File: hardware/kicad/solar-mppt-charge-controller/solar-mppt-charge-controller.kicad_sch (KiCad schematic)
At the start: 0 parts

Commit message: Schematic: LM2596 buck converter power stage complete
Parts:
- added C1: 100uF, symbol Device:C
- added C2: 220uF, symbol Device:C
- added D1, D2: 1N5822, symbol Device:D
- added F1: Fuse, symbol Device:Fuse
- added J1: SOLAR_IN, symbol Connector_Generic:Conn_01x02
- added J2: LOAD_OUT, symbol Connector_Generic:Conn_01x02
- added L1: 100uH, symbol Device:L
- added R1: 100k, symbol Device:R
- added R2: 10k, symbol Device:R
- added U1: LM2596S-ADJ, Package_TO_SOT_SMD:TO-263-5_TabPin3, symbol Regulator_Switching:LM2596S-ADJ
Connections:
- new net: R1.1, R2.1, U1.4 (FB)
- new net: L1.2, U1.2 (OUT)
- new net: D1.2 (A), F1.1, F1.2, J1.1 (Pin_1)
- new net GND: C1.1, C2.2, D2.2 (A), J1.2 (Pin_2), J2.2 (Pin_2), R2.2, U1.3 (GND), U1.5 (~{ON}/OFF)
- new net PANEL_IN: C1.2, D1.1 (K), U1.1 (VIN)
- new net VOUT: C2.1, D2.1 (K), J2.1 (Pin_1), L1.1, R1.2

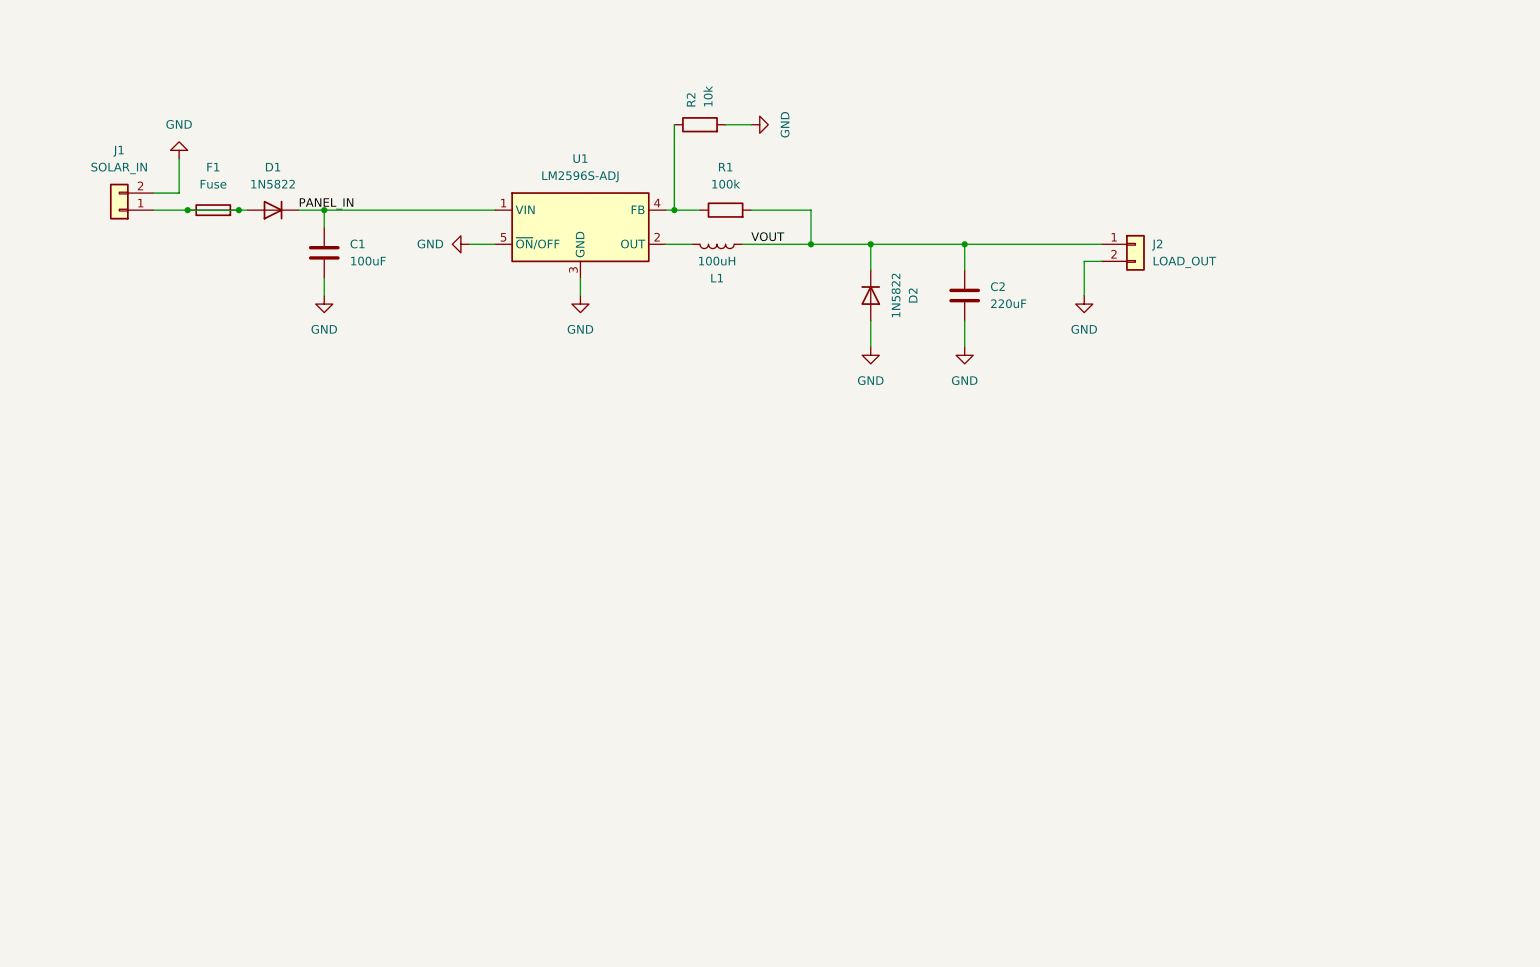
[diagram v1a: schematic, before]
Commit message: Schematic: MCP4131 digital potentiometer complete
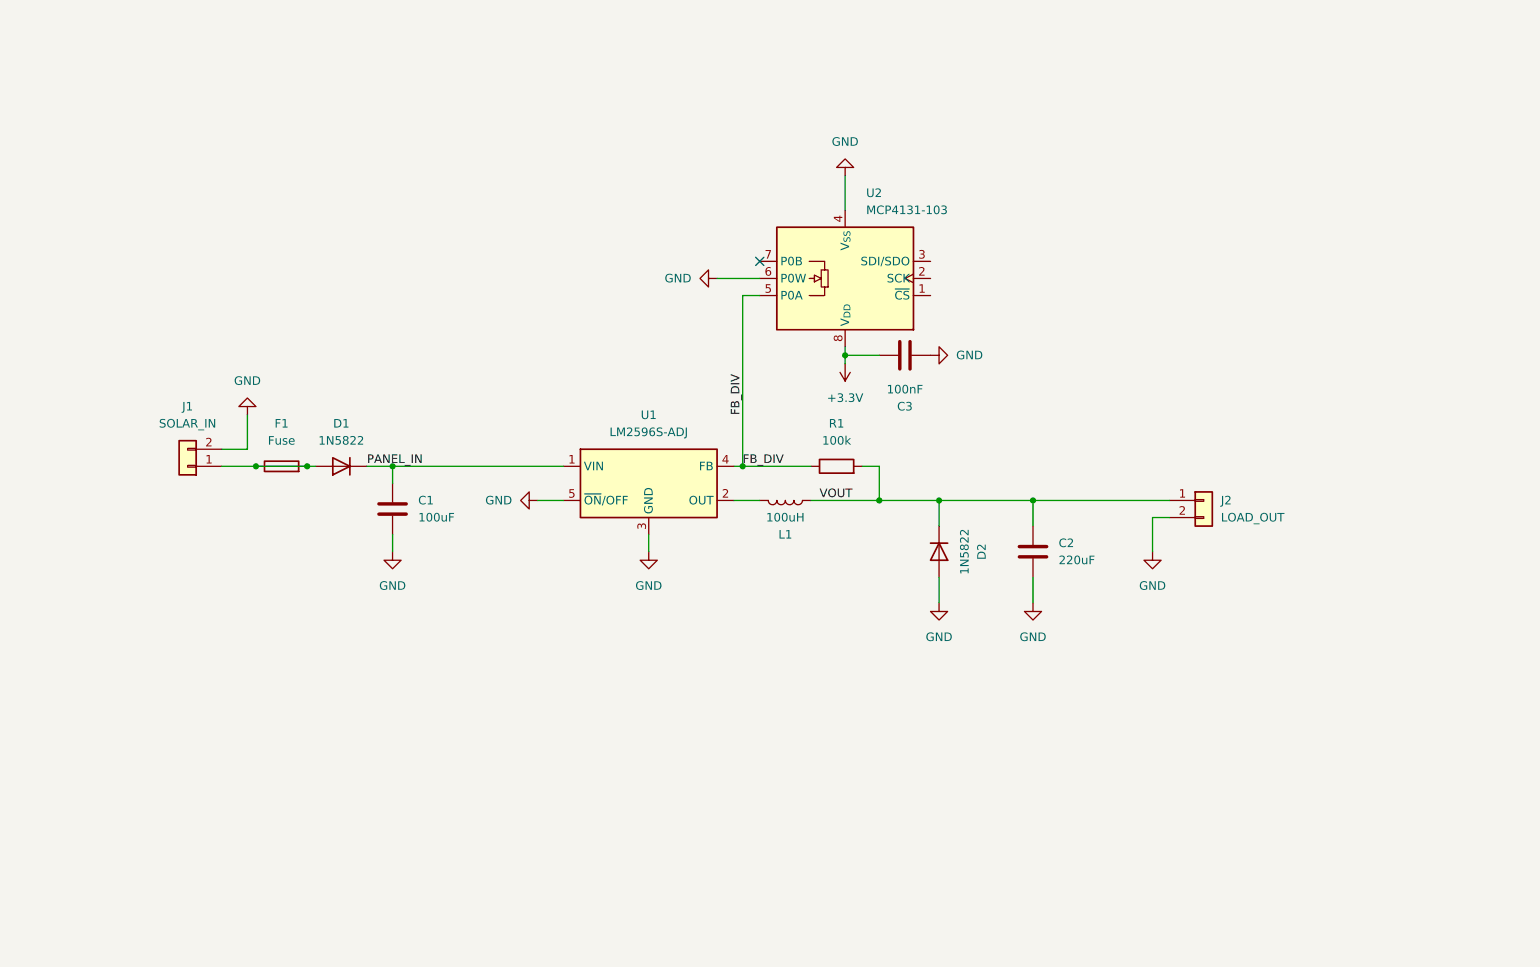
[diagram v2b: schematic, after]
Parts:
- removed R2: 10k, symbol Device:R
- added C3: 100nF, symbol Device:C
- added U2: MCP4131-103, Package_DIP:DIP-8_W7.62mm, symbol Potentiometer_Digital:MCP4131-xxxx-P
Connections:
- net GND: now also C3.1, U2.4 (V_{SS}), U2.6 (P0W)
- net FB_DIV: now reaches R1.1, U1.4 (FB)
- net FB_DIV: now also U2.5 (P0A)
- new net +3.3V: C3.2, U2.8 (V_{DD})
- no-connect marks 0 -> 1
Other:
- moved on the sheet: C1, C2, D1, D2, F1, J1, J2, L1, R1, U1

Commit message: Schematic: ESP32 DevKit connector and UART debug header complete
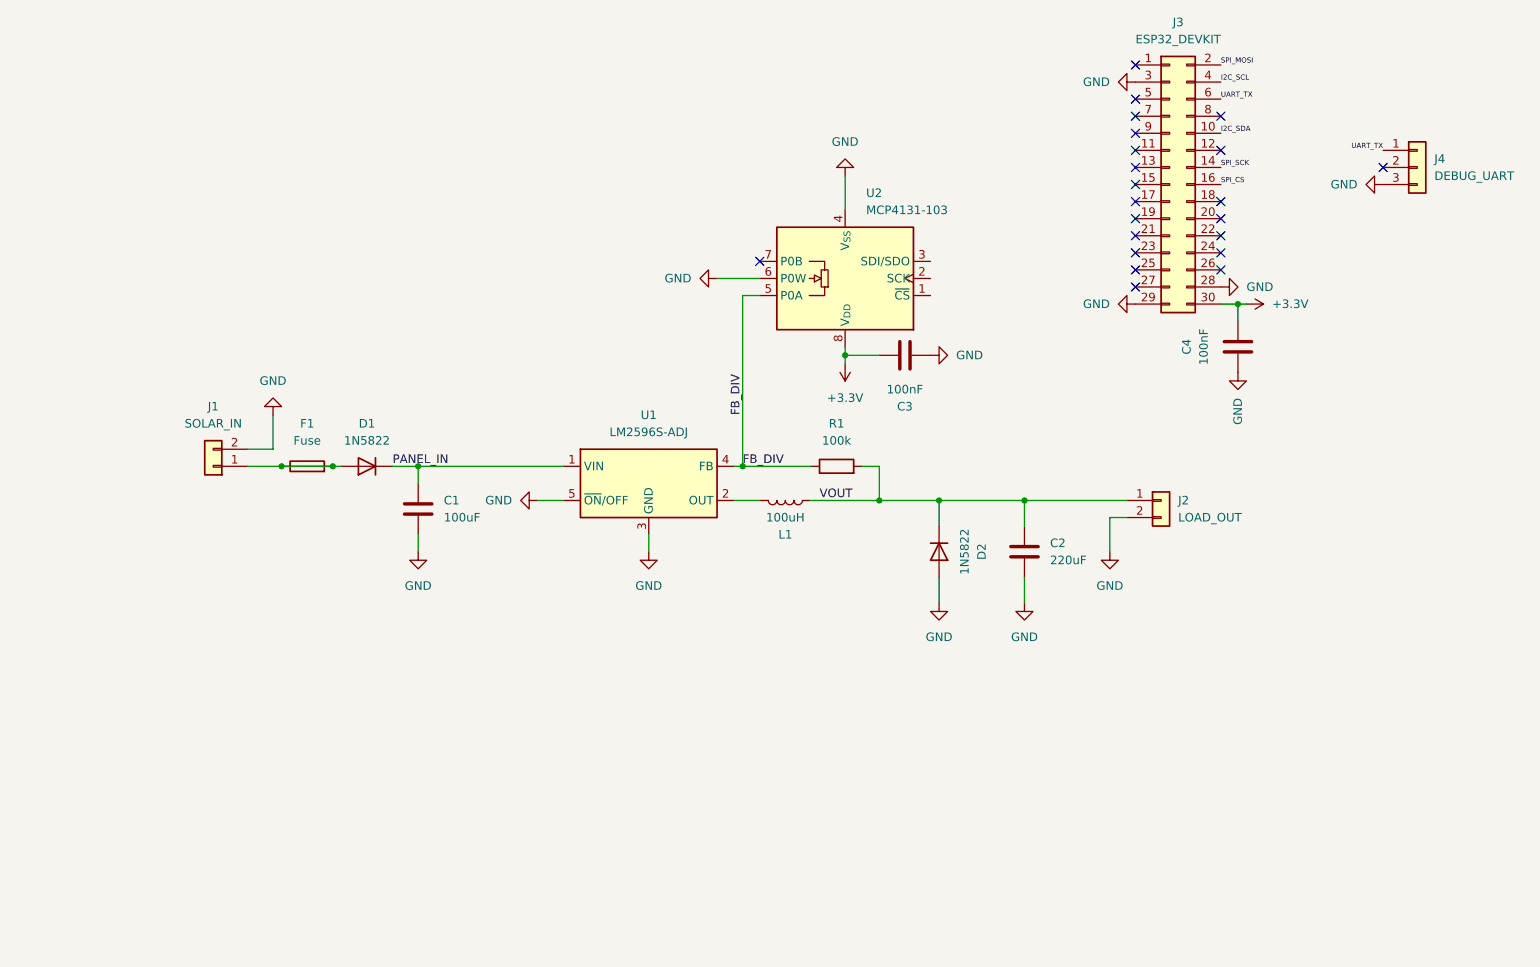
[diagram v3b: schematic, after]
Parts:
- added C4: 100nF, symbol Device:C
- added J3: ESP32_DEVKIT, symbol Connector_Generic:Conn_02x15_Odd_Even
- added J4: DEBUG_UART, symbol Connector_Generic:Conn_01x03
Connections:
- net +3.3V: now also C4.2, J3.30 (Pin_30)
- net GND: now also C4.1, J3.28 (Pin_28), J3.29 (Pin_29), J3.3 (Pin_3), J4.3 (Pin_3)
- new net I2C_SCL: J3.4 (Pin_4)
- new net I2C_SDA: J3.10 (Pin_10)
- new net SPI_CS: J3.16 (Pin_16)
- new net SPI_MOSI: J3.2 (Pin_2)
- new net SPI_SCK: J3.14 (Pin_14)
- new net UART_TX: J3.6 (Pin_6), J4.1 (Pin_1)
- no-connect marks 1 -> 22
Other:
- moved on the sheet: C1, C2, D1, F1, J1, J2

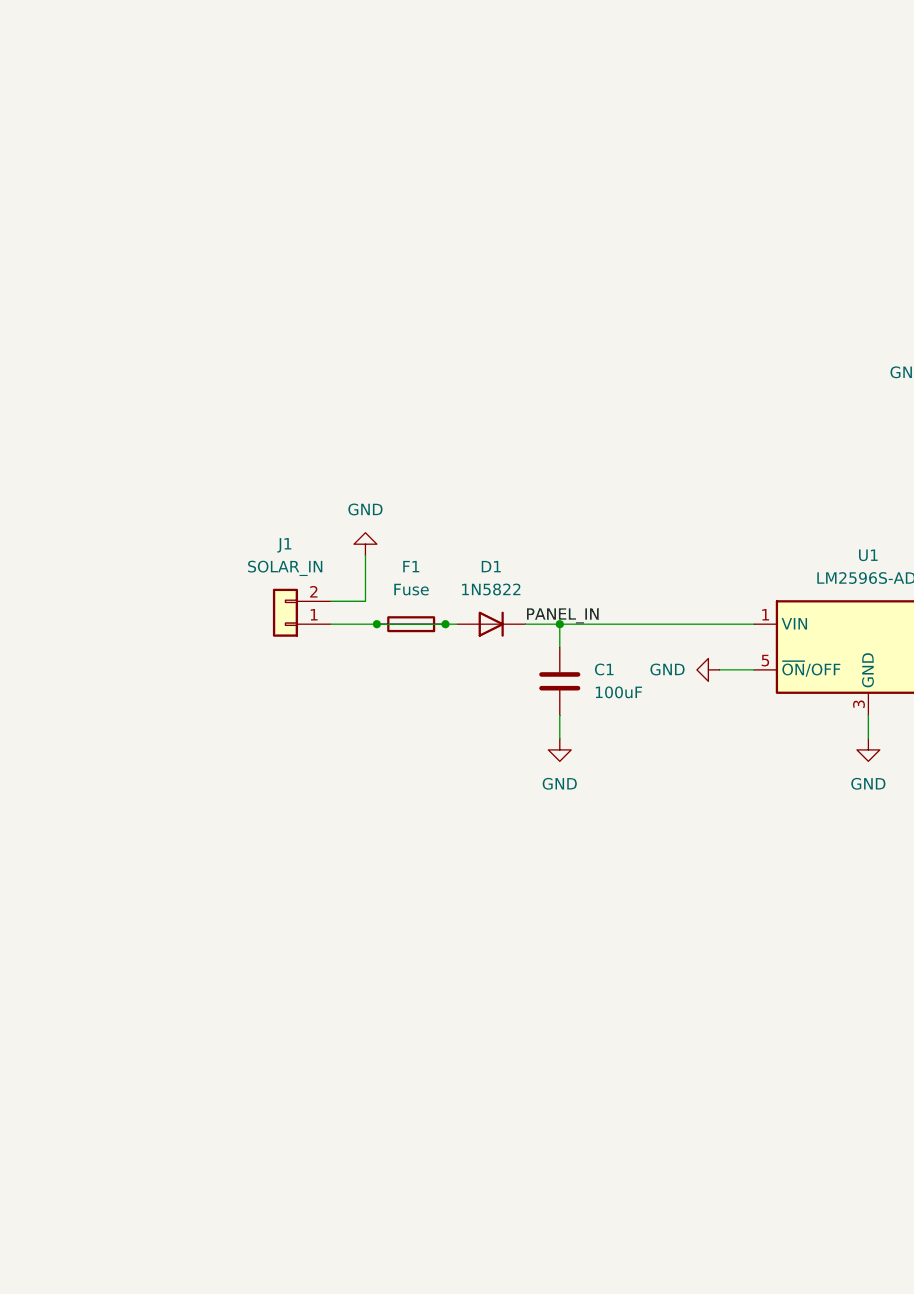
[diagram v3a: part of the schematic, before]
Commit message: Schematic: INA226 panel and load side sensors complete
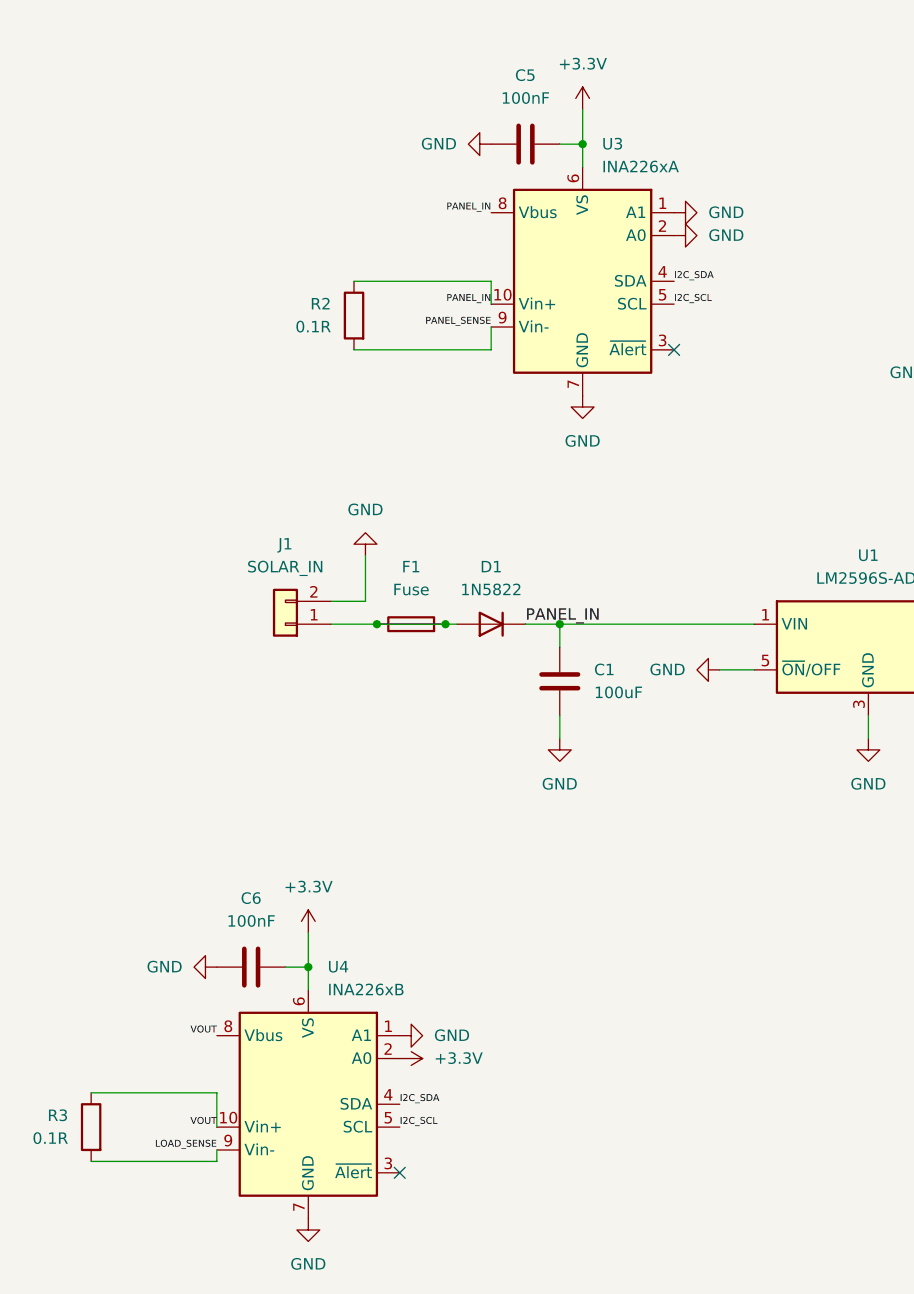
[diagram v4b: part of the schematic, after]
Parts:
- added C5, C6: 100nF, symbol Device:C
- added R2, R3: 0.1R, symbol Device:R
- added U3: INA226xA, Package_SO:TSSOP-10_3x3mm_P0.5mm, symbol Sensor_Energy:INA226
- added U4: INA226xB, Package_SO:TSSOP-10_3x3mm_P0.5mm, symbol Sensor_Energy:INA226
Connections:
- net +3.3V: now also C5.2, C6.2, U3.6 (VS), U4.2 (A0), U4.6 (VS)
- net GND: now also C5.1, C6.1, U3.1 (A1), U3.2 (A0), U3.7 (GND), U4.1 (A1), U4.7 (GND)
- net I2C_SCL: now also U3.5 (SCL), U4.5 (SCL)
- net I2C_SDA: now also U3.4 (SDA), U4.4 (SDA)
- net PANEL_IN: now also R2.1, U3.10 (Vin+), U3.8 (Vbus)
- net VOUT: now also R3.1, U4.10 (Vin+), U4.8 (Vbus)
- new net LOAD_SENSE: R3.2, U4.9 (Vin-)
- new net PANEL_SENSE: R2.2, U3.9 (Vin-)
- no-connect marks 22 -> 24

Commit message: Schematic: ERC clean, zero errors and warnings
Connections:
- net SPI_CS: now also U2.1 (~{CS})
- net SPI_MOSI: now also U2.3 (SDI/SDO)
- net SPI_SCK: now also U2.2 (SCK)

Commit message: Footprints assigned to all schematic components
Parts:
- C1: footprint (none) -> Capacitor_THT:C_Radial_D8.0mm_H7.0mm_P3.50mm
- C2: footprint (none) -> Capacitor_THT:C_Radial_D10.0mm_H12.5mm_P5.00mm
- C3, C4, C5, C6: footprint (none) -> Capacitor_SMD:C_0805_2012Metric_Pad1.18x1.45mm_HandSolder
- D1, D2: footprint (none) -> Diode_THT:D_DO-201AD_P12.70mm_Horizontal
- F1: footprint (none) -> Fuse:Fuse_1812_4532Metric_Pad1.30x3.40mm_HandSolder
- J1, J2: footprint (none) -> Connector_PinHeader_2.54mm:PinHeader_1x02_P2.54mm_Vertical
- J3: footprint (none) -> Connector_PinHeader_2.54mm:PinHeader_2x15_P2.54mm_Vertical
- J4: footprint (none) -> Connector_PinHeader_2.54mm:PinHeader_1x03_P2.54mm_Vertical
- L1: footprint (none) -> Inductor_THT:L_Axial_L11.0mm_D4.5mm_P15.24mm_Horizontal_Fastron_MECC
- R1: footprint (none) -> Resistor_SMD:R_0805_2012Metric_Pad1.20x1.40mm_HandSolder
- R2, R3: footprint (none) -> Resistor_SMD:R_2512_6332Metric_Pad1.40x3.35mm_HandSolder
- U3, U4: footprint Package_SO:TSSOP-10_3x3mm_P0.5mm -> Package_SO:SOIC-10_3.9x4.9mm_P1mm
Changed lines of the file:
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@@
 			)
 		)
-		(property "Footprint" ""
+		(property "Footprint" "Capacitor_THT:C_Radial_D8.0mm_H7.0mm_P3.50mm"
 			(at 104.4448 101.6 0)
 			(hide yes)
@@
 			)
 		)
-		(property "Footprint" ""
+		(property "Footprint" "Resistor_SMD:R_2512_6332Metric_Pad1.40x3.35mm_HandSolder"
 			(at 84.328 64.77 90)
 			(hide yes)
@@
 			)
 		)
-		(property "Footprint" ""
+		(property "Footprint" "Resistor_SMD:R_0805_2012Metric_Pad1.20x1.40mm_HandSolder"
 			(at 167.64 100.838 90)
 			(hide yes)
@@
 			)
 		)
-		(property "Footprint" ""
+		(property "Footprint" "Inductor_THT:L_Axial_L11.0mm_D4.5mm_P15.24mm_Horizontal_Fastron_MECC"
 			(at 160.02 104.14 0)
 			(hide yes)
@@
 			)
 		)
-		(property "Footprint" ""
+		(property "Footprint" "Fuse:Fuse_1812_4532Metric_Pad1.30x3.40mm_HandSolder"
 			(at 88.9 100.838 90)
 			(hide yes)
@@
 			)
 		)
-		(property "Footprint" ""
+		(property "Footprint" "Connector_PinHeader_2.54mm:PinHeader_2x15_P2.54mm_Vertical"
 			(at 217.17 57.15 0)
 			(hide yes)
@@
 			)
 		)
-		(property "Footprint" "Package_SO:TSSOP-10_3x3mm_P0.5mm"
+		(property "Footprint" "Package_SO:SOIC-10_3.9x4.9mm_P1mm"
 			(at 128.27 72.39 0)
 			(hide yes)
@@
 			)
 		)
-		(property "Footprint" ""
+		(property "Footprint" "Diode_THT:D_DO-201AD_P12.70mm_Horizontal"
 			(at 97.79 99.06 0)
 			(hide yes)
@@
 			)
 		)
-		(property "Footprint" ""
+		(property "Footprint" "Capacitor_THT:C_Radial_D10.0mm_H12.5mm_P5.00mm"
 			(at 196.5452 115.57 0)
 			(hide yes)
@@
 			)
 		)
-		(property "Footprint" ""
+		(property "Footprint" "Connector_PinHeader_2.54mm:PinHeader_1x02_P2.54mm_Vertical"
 			(at 215.9 104.14 0)
 			(hide yes)
@@
 			)
 		)
-		(property "Footprint" ""
+		(property "Footprint" "Capacitor_SMD:C_0805_2012Metric_Pad1.18x1.45mm_HandSolder"
 			(at 226.3648 77.47 0)
 			(hide yes)
@@
 			)
 		)
-		(property "Footprint" ""
+		(property "Footprint" "Capacitor_SMD:C_0805_2012Metric_Pad1.18x1.45mm_HandSolder"
 			(at 105.41 44.7548 0)
 			(hide yes)
@@
 			)
 		)
-		(property "Footprint" "Package_SO:TSSOP-10_3x3mm_P0.5mm"
+		(property "Footprint" "Package_SO:SOIC-10_3.9x4.9mm_P1mm"
 			(at 97.79 163.83 0)
 			(hide yes)
@@
 			)
 		)
-		(property "Footprint" ""
+		(property "Footprint" "Connector_PinHeader_2.54mm:PinHeader_1x02_P2.54mm_Vertical"
 			(at 74.93 99.06 0)
 			(hide yes)
@@
 			)
 		)
-		(property "Footprint" ""
+		(property "Footprint" "Resistor_SMD:R_2512_6332Metric_Pad1.40x3.35mm_HandSolder"
 			(at 55.118 154.94 90)
 			(hide yes)
@@
 			)
 		)
-		(property "Footprint" ""
+		(property "Footprint" "Capacitor_SMD:C_0805_2012Metric_Pad1.18x1.45mm_HandSolder"
 			(at 173.99 83.5152 0)
 			(hide yes)
@@
 			)
 		)
-		(property "Footprint" ""
+		(property "Footprint" "Diode_THT:D_DO-201AD_P12.70mm_Horizontal"
 			(at 182.88 111.76 0)
 			(hide yes)
@@
 			)
 		)
-		(property "Footprint" ""
+		(property "Footprint" "Capacitor_SMD:C_0805_2012Metric_Pad1.18x1.45mm_HandSolder"
 			(at 74.93 136.1948 0)
 			(hide yes)
@@
 			)
 		)
-		(property "Footprint" ""
+		(property "Footprint" "Connector_PinHeader_2.54mm:PinHeader_1x03_P2.54mm_Vertical"
 			(at 254 54.61 0)
 			(hide yes)

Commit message: PCB: routing complete, GND vias and F1 net issue remaining
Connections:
- net FUSE_OUT: now reaches D1.2 (A), F1.1, F1.2, J1.1 (Pin_1)
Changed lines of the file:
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@@
+		)
+	)
+	(label "FUSE_OUT"
+		(at 93.98 99.06 270)
+		(effects
+			(font
+				(size 0.508 0.508)
+			)
+			(justify right bottom)
 		)
 	)
